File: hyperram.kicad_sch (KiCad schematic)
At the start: 7 parts, among them U11 S27KL0641DABHI023

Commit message: [#80386] Add company name in board settings
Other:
- company: Antmicro Ltd. -> Antmicro
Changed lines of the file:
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@@
 		(date "2023-07-27")
 		(rev "1.0.1")
-		(company "Antmicro Ltd.")
+		(company "Antmicro")
 		(comment 1 "www.antmicro.com")
-		(comment 2 "Antmicro Ltd")
 	)
 	(text "HyperRAM"

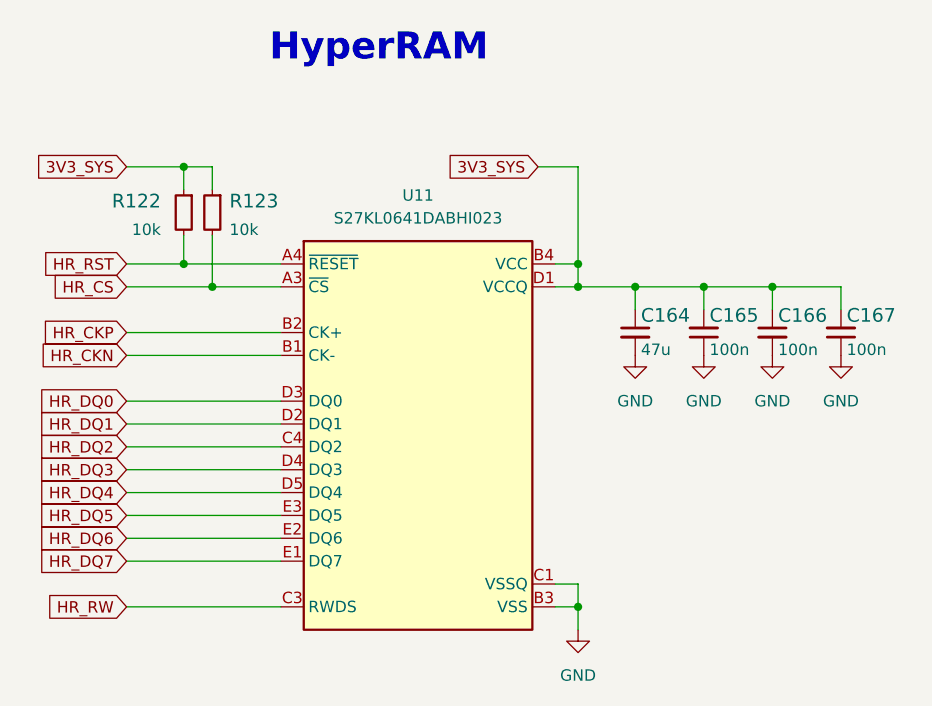
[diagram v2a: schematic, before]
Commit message: [#87036] Update components, clear DRC and ERC
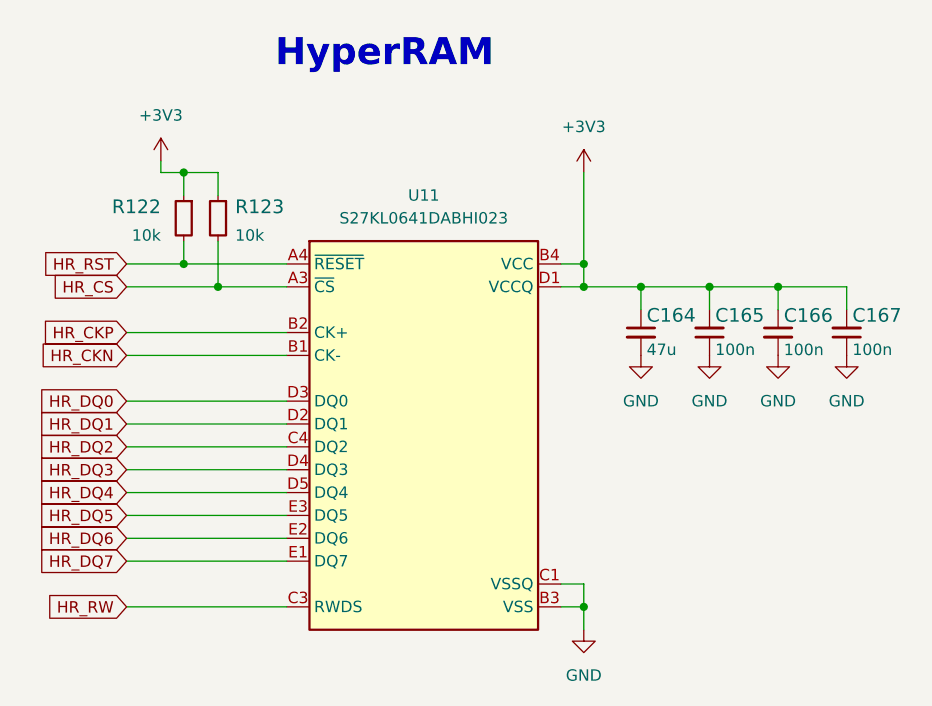
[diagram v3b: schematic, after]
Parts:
- C164: footprint data-center-rdimm-ddr5-tester-footprints:C_0603_1608Metric -> antmicro-footprints:C_0603_1608Metric; symbol data-center-rdimm-ddr5-tester:C_47u_0603 -> antmicroCapacitors0603:C_47u_0603
- C165, C166, C167: footprint data-center-rdimm-ddr5-tester-footprints:C_0402_1005Metric -> antmicro-footprints:C_0402_1005Metric; symbol data-center-rdimm-ddr5-tester:C_100n_6V3_0402 -> antmicroCapacitorsmisc:C_100n_6V3_0402; Public (none) -> False
- R122, R123: footprint data-center-rdimm-ddr5-tester-footprints:R_0402_1005Metric -> antmicro-footprints:R_0402_1005Metric; symbol data-center-rdimm-ddr5-tester:R_10k_0402 -> antmicroResistors0402:R_10k_0402
- U11: footprint data-center-rdimm-ddr5-tester-footprints:FBGA-24-1_6x8mm_Layout5x5_P1mm -> antmicro-footprints:FBGA-25-24_6x8mm_Layout5x5_P1mm; symbol data-center-rdimm-ddr5-tester:S27KL0641DABHI023 -> antmicroMemory:S27KL0641DABHI023
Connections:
- net 3V3_SYS renamed +3V3
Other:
- moved on the sheet: C164, C165, C166, C167, R122, R123, U11
